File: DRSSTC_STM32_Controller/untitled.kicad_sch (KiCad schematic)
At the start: 46 parts, among them J4 Screw_Terminal_01x02, U3 LF15_TO252, U4 TPS54560BDDA, U7 LV2842XLVDDCR

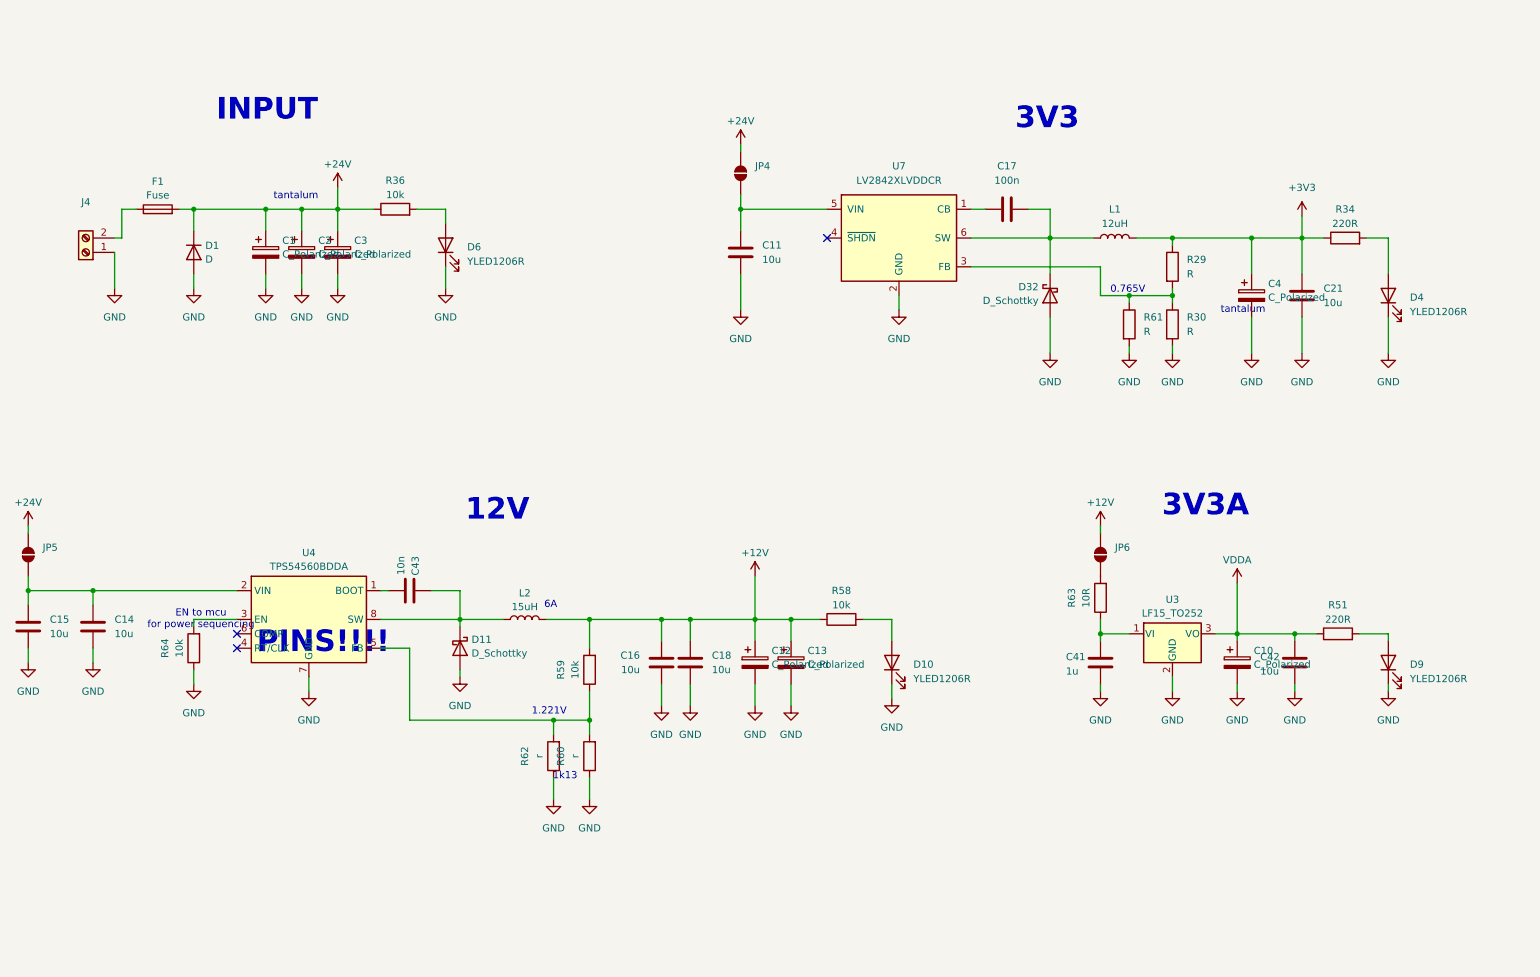
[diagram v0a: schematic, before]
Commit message: update the feedback stage simulation & controller schematic
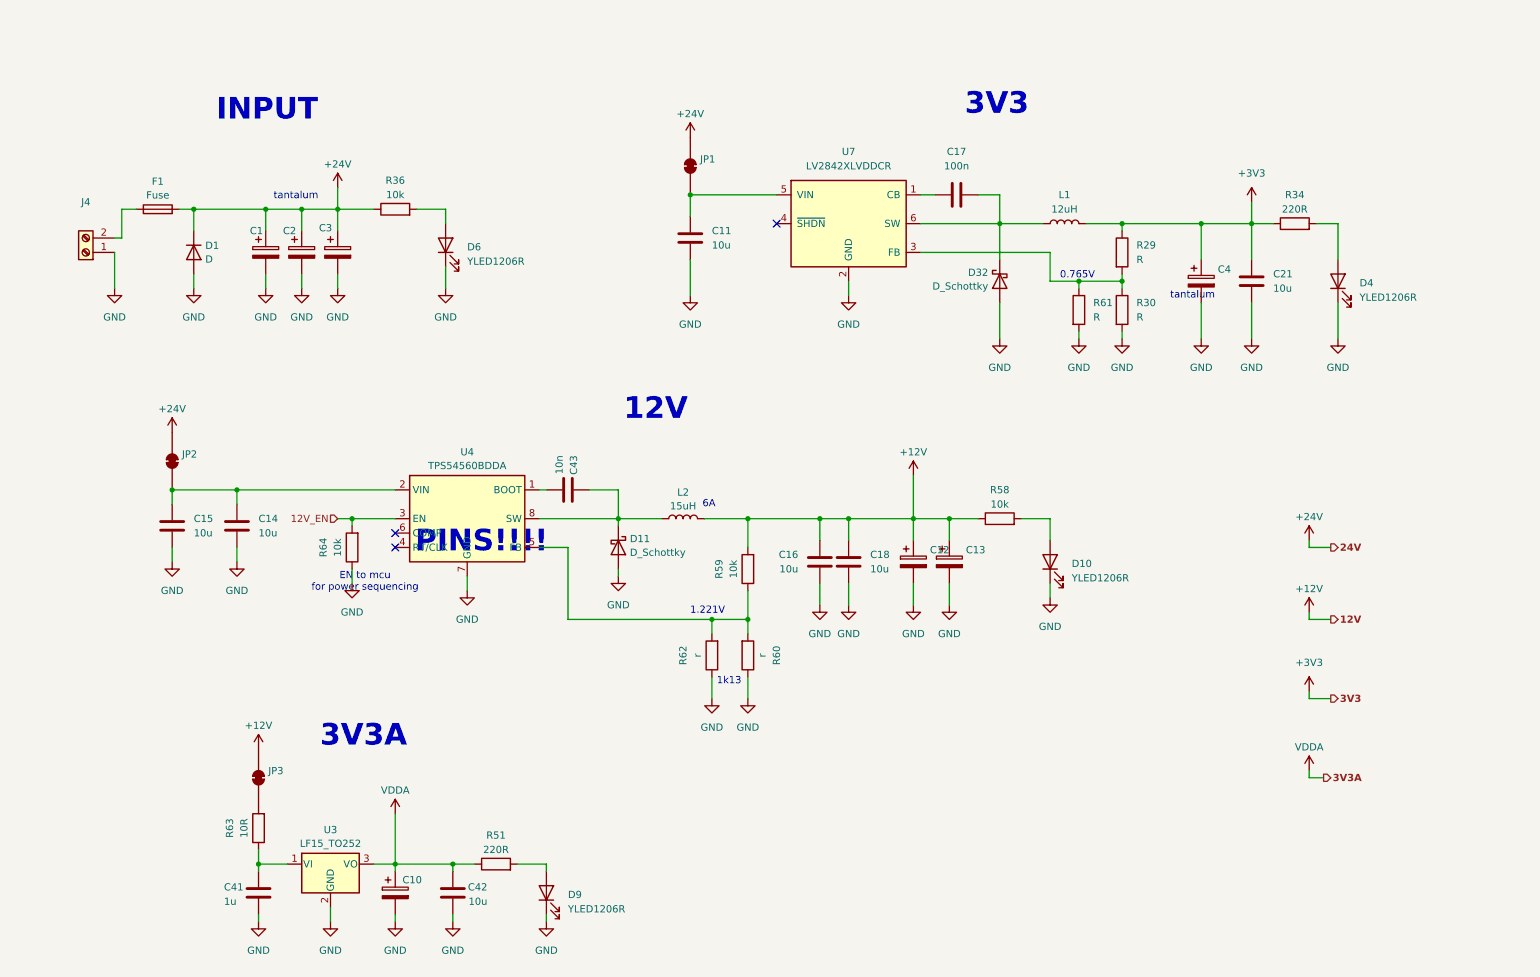
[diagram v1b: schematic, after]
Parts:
- removed JP4, JP5, JP6: SolderJumper_2_Open, Jumper:SolderJumper-2_P1.3mm_Open_RoundedPad1.0x1.5mm, symbol Jumper:SolderJumper_2_Open
- added JP1, JP2, JP3: SolderJumper_2_Bridged, symbol Jumper:SolderJumper_2_Bridged
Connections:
- net +12V: now also JP3.2 (B)
- net +24V: now also JP1.2 (B), JP2.2 (B)
- net at C14.1, C15.1, U4.2 (VIN): now also JP2.1 (A)
- net 12V_EN: now reaches R64.2, U4.3 (EN)
- net at C11.1, U7.5 (VIN): now also JP1.1 (A)
- net at R63.2: now also JP3.1 (A)
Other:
- moved on the sheet: C10, C11, C12, C13, C14, C15, C16, C17, C18, C21, C4, C41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

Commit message: update conroller schematics
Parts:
- removed J4: Screw_Terminal_01x02, TerminalBlock_Altech:Altech_AK100_1x02_P5.00mm, symbol Connector:Screw_Terminal_01x02
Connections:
- net 24Vin: now reaches F1.1
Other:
- note removed: "EN to mcu for power sequencing"
- moved on the sheet: C1, C10, C11, C12, C13, C14, C15, C16, C17, C18, C2, C21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

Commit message: assign footprints
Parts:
- removed D1: D, symbol Device:D
- added C5: C_Polarized, Capacitor_Tantalum_SMD:CP_EIA-3528-12_Kemet-T, symbol Device:C_Polarized
- added D49: D_Schottky, Diode_SMD:D_SOD-128, symbol Device:D_Schottky
- C1, C12, C13, C2, C3: footprint (none) -> Capacitor_SMD:CP_Elec_10x10
- C10, C4: footprint (none) -> Capacitor_Tantalum_SMD:CP_EIA-3528-12_Kemet-T
- C17, C41, C43: footprint Capacitor_SMD:C_0805_2012Metric -> Capacitor_SMD:C_0603_1608Metric
- D11, D32: footprint (none) -> Diode_SMD:D_SOD-128
- F1: footprint (none) -> Fuse:Fuse_2512_6332Metric
- JP1, JP2, JP3: footprint (none) -> Jumper:SolderJumper-2_P1.3mm_Bridged2Bar_RoundedPad1.0x1.5mm
- L2: footprint (none) -> Inductor_SMD:L_10.4x10.4_H4.8
- R29, R30, R59, R60, R61, R62, R64: footprint Resistor_SMD:R_0805_2012Metric -> Resistor_SMD:R_0603_1608Metric
- U3: footprint Package_TO_SOT_SMD:TO-252-2 -> Package_TO_SOT_SMD:TO-252-3_TabPin2
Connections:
- net +24V: now also D49.1 (K)
- net +3V3: now also C5.1
- net GND: now also C5.2, D49.2 (A)
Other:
- moved on the sheet: C21, D4, R34

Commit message: start cintrollenr routing
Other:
- note removed: "PINS!!!!"
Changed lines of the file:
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@@
-		)
-	)
-	(text "PINS!!!!"
-		(exclude_from_sim no)
-		(at 104.648 136.652 0)
-		(effects
-			(font
-				(size 3.81 3.81)
-				(thickness 0.762)
-				(bold yes)
-			)
 		)
 	)
